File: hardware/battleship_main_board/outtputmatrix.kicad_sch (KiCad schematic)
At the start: 0 parts

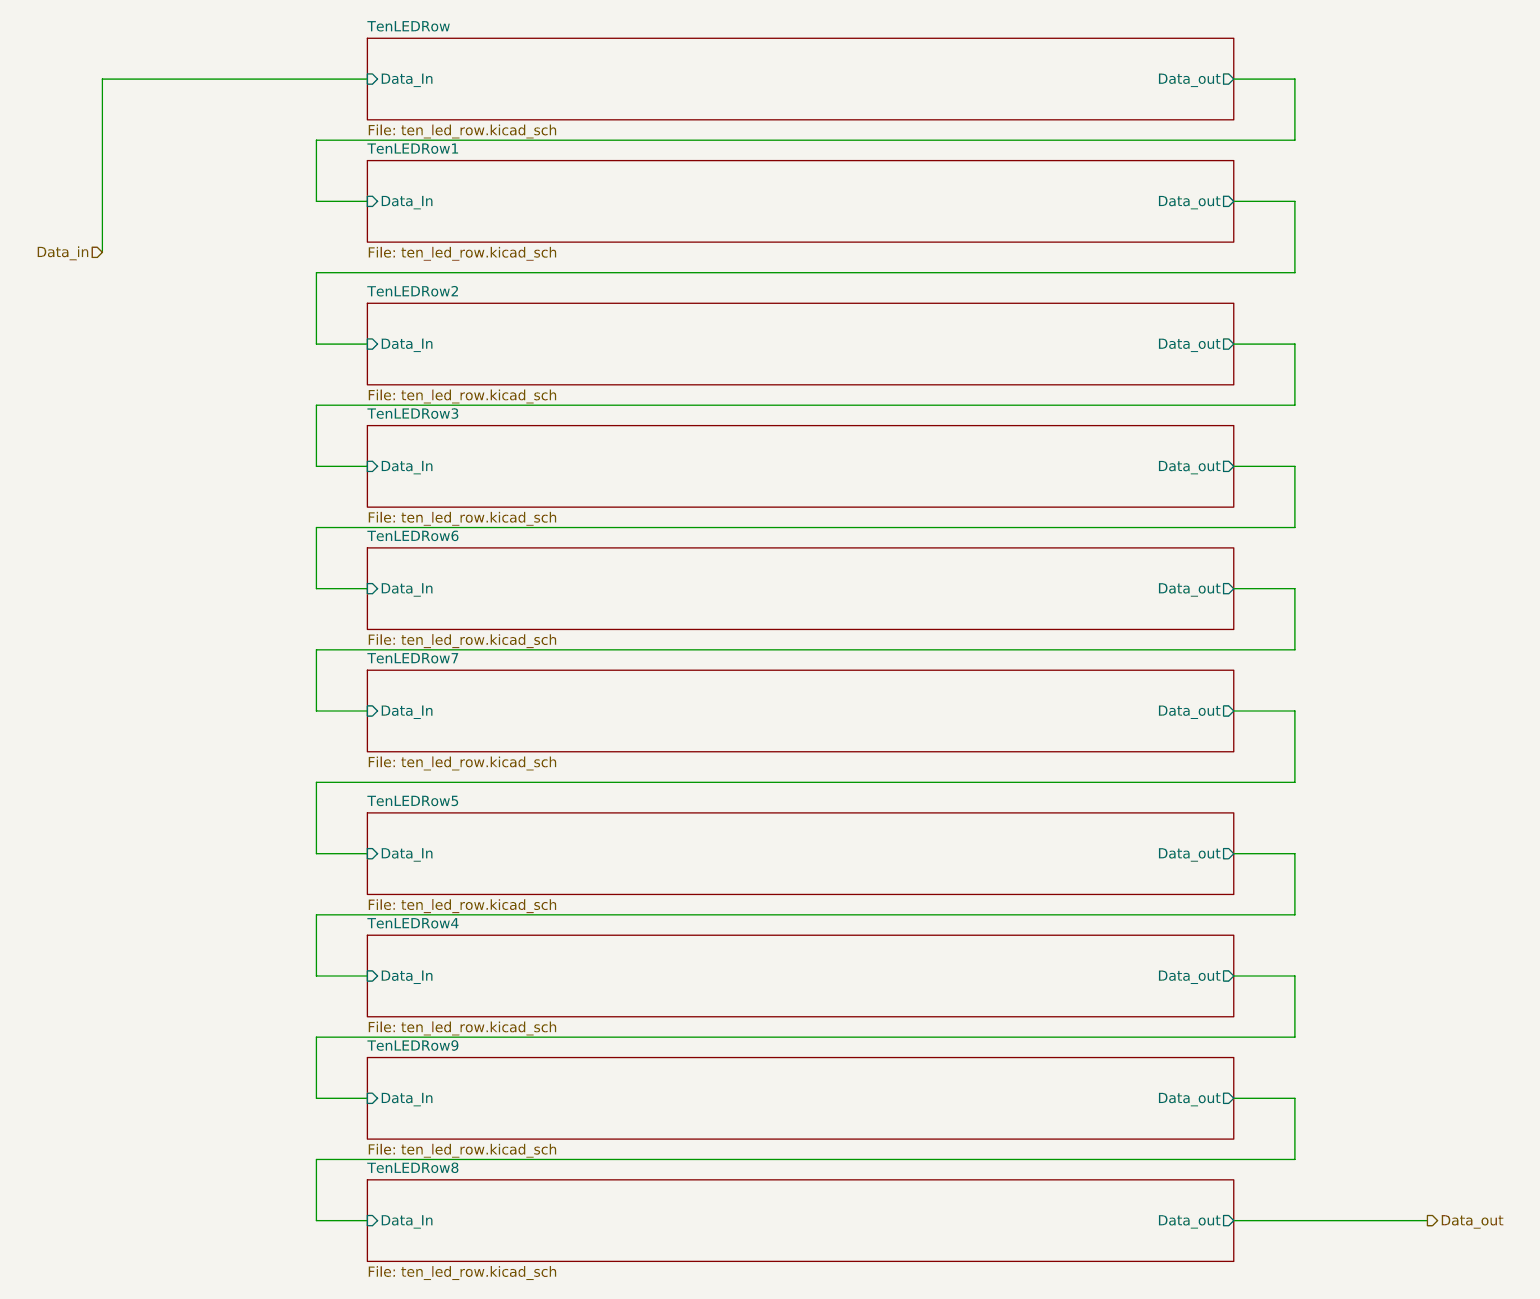
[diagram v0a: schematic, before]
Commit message: Got schematic to place that can be turned into a ratsnest
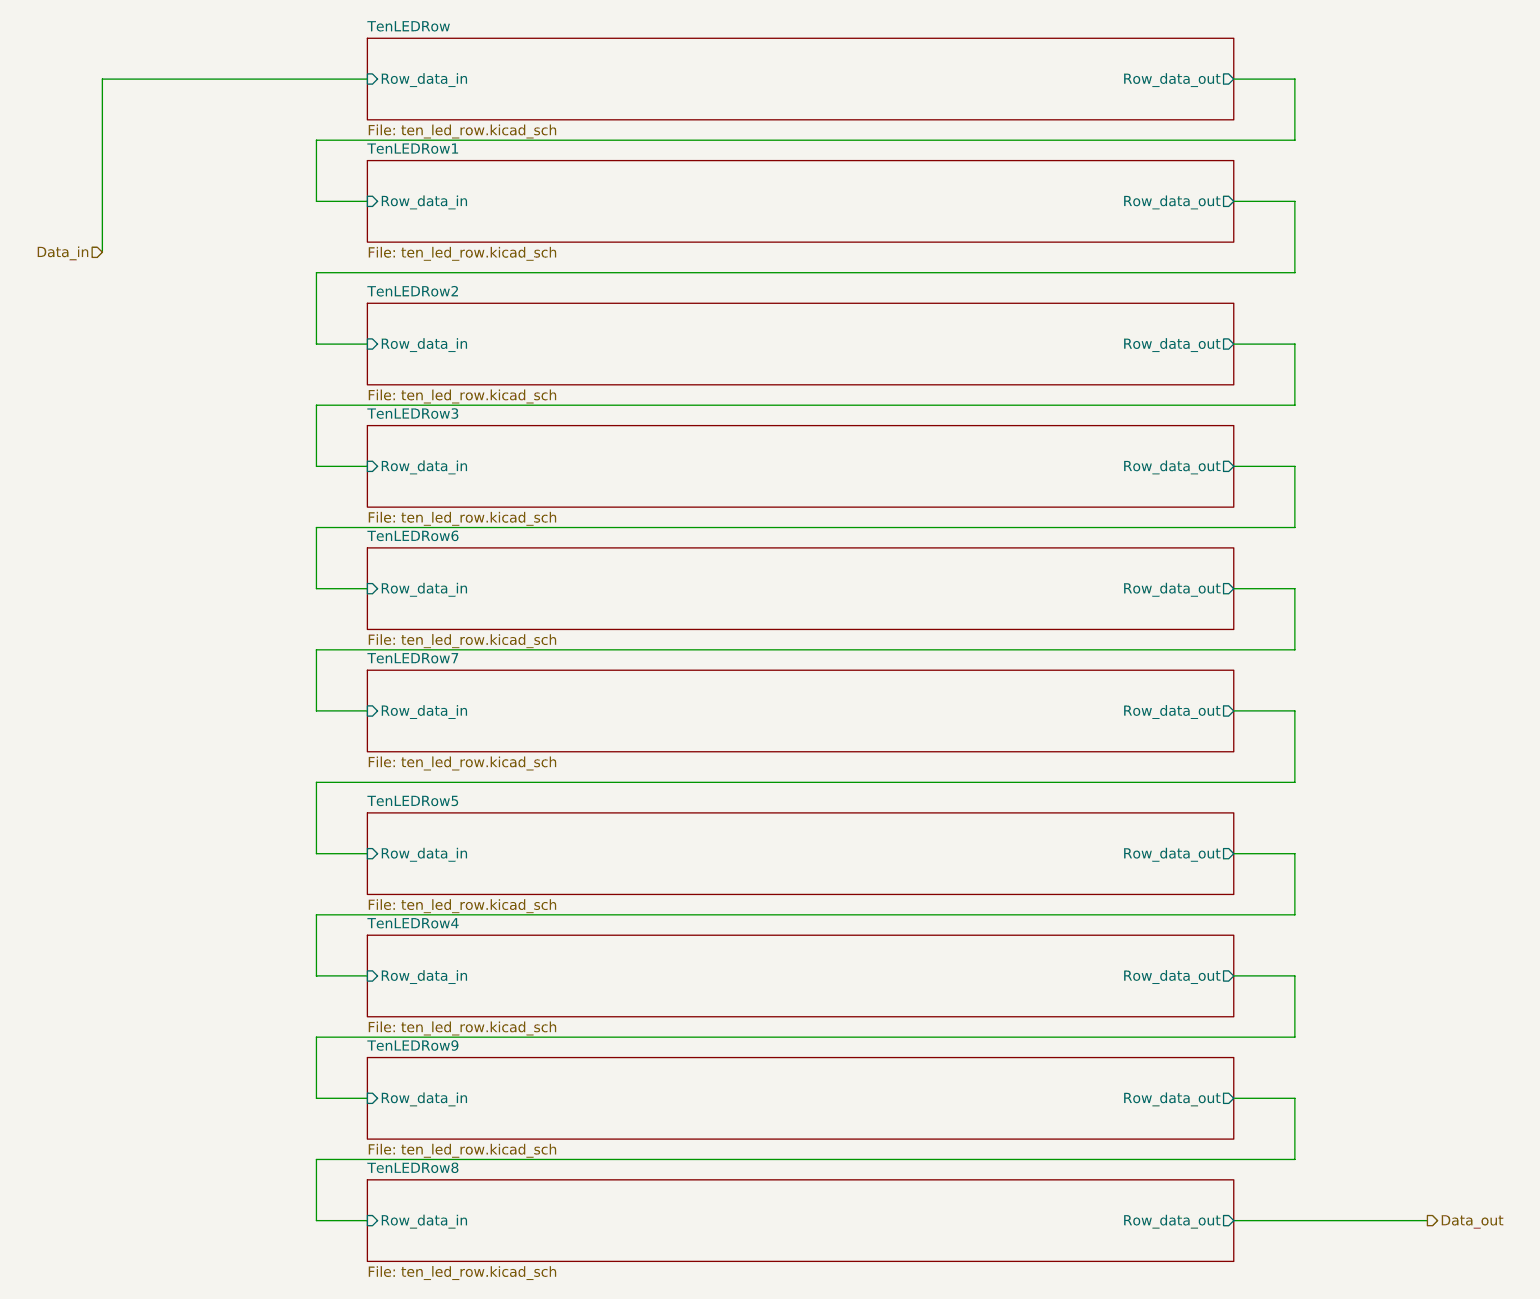
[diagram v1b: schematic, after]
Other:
- sheet TenLEDRow ports: added Row_data_in, Row_data_out; removed Data_In, Data_out
- sheet TenLEDRow1 ports: added Row_data_in, Row_data_out; removed Data_In, Data_out
- sheet TenLEDRow2 ports: added Row_data_in, Row_data_out; removed Data_In, Data_out
- sheet TenLEDRow3 ports: added Row_data_in, Row_data_out; removed Data_In, Data_out
- sheet TenLEDRow4 ports: added Row_data_in, Row_data_out; removed Data_In, Data_out
- sheet TenLEDRow5 ports: added Row_data_in, Row_data_out; removed Data_In, Data_out
- sheet TenLEDRow6 ports: added Row_data_in, Row_data_out; removed Data_In, Data_out
- sheet TenLEDRow7 ports: added Row_data_in, Row_data_out; removed Data_In, Data_out
- sheet TenLEDRow8 ports: added Row_data_in, Row_data_out; removed Data_In, Data_out
- sheet TenLEDRow9 ports: added Row_data_in, Row_data_out; removed Data_In, Data_out
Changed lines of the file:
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@@
       (effects (font (size 1.27 1.27)) (justify left top))
     )
-    (pin "Data_out" output (at 165.1 85.09 0)
+    (pin "Row_data_out" output (at 165.1 85.09 0)
       (effects (font (size 1.27 1.27)) (justify right))
     )
-    (pin "Data_In" input (at 57.15 85.09 180)
+    (pin "Row_data_in" input (at 57.15 85.09 180)
       (effects (font (size 1.27 1.27)) (justify left))
     )
@@
       (effects (font (size 1.27 1.27)) (justify left top))
     )
-    (pin "Data_out" output (at 165.1 148.59 0)
+    (pin "Row_data_out" output (at 165.1 148.59 0)
       (effects (font (size 1.27 1.27)) (justify right))
     )
-    (pin "Data_In" input (at 57.15 148.59 180)
+    (pin "Row_data_in" input (at 57.15 148.59 180)
       (effects (font (size 1.27 1.27)) (justify left))
     )
@@
       (effects (font (size 1.27 1.27)) (justify left top))
     )
-    (pin "Data_out" output (at 165.1 133.35 0)
+    (pin "Row_data_out" output (at 165.1 133.35 0)
       (effects (font (size 1.27 1.27)) (justify right))
     )
-    (pin "Data_In" input (at 57.15 133.35 180)
+    (pin "Row_data_in" input (at 57.15 133.35 180)
       (effects (font (size 1.27 1.27)) (justify left))
     )
@@
       (effects (font (size 1.27 1.27)) (justify left top))
     )
-    (pin "Data_out" output (at 165.1 69.85 0)
+    (pin "Row_data_out" output (at 165.1 69.85 0)
       (effects (font (size 1.27 1.27)) (justify right))
     )
-    (pin "Data_In" input (at 57.15 69.85 180)
+    (pin "Row_data_in" input (at 57.15 69.85 180)
       (effects (font (size 1.27 1.27)) (justify left))
     )
@@
       (effects (font (size 1.27 1.27)) (justify left top))
     )
-    (pin "Data_out" output (at 165.1 21.59 0)
+    (pin "Row_data_out" output (at 165.1 21.59 0)
       (effects (font (size 1.27 1.27)) (justify right))
     )
-    (pin "Data_In" input (at 57.15 21.59 180)
+    (pin "Row_data_in" input (at 57.15 21.59 180)
       (effects (font (size 1.27 1.27)) (justify left))
     )
@@
       (effects (font (size 1.27 1.27)) (justify left top))
     )
-    (pin "Data_out" output (at 165.1 36.83 0)
+    (pin "Row_data_out" output (at 165.1 36.83 0)
       (effects (font (size 1.27 1.27)) (justify right))
     )
-    (pin "Data_In" input (at 57.15 36.83 180)
+    (pin "Row_data_in" input (at 57.15 36.83 180)
       (effects (font (size 1.27 1.27)) (justify left))
     )
@@
       (effects (font (size 1.27 1.27)) (justify left top))
     )
-    (pin "Data_out" output (at 165.1 54.61 0)
+    (pin "Row_data_out" output (at 165.1 54.61 0)
       (effects (font (size 1.27 1.27)) (justify right))
     )
-    (pin "Data_In" input (at 57.15 54.61 180)
+    (pin "Row_data_in" input (at 57.15 54.61 180)
       (effects (font (size 1.27 1.27)) (justify left))
     )
@@
       (effects (font (size 1.27 1.27)) (justify left top))
     )
-    (pin "Data_out" output (at 165.1 100.33 0)
+    (pin "Row_data_out" output (at 165.1 100.33 0)
       (effects (font (size 1.27 1.27)) (justify right))
     )
-    (pin "Data_In" input (at 57.15 100.33 180)
+    (pin "Row_data_in" input (at 57.15 100.33 180)
       (effects (font (size 1.27 1.27)) (justify left))
     )
@@
       (effects (font (size 1.27 1.27)) (justify left top))
     )
-    (pin "Data_out" output (at 165.1 118.11 0)
+    (pin "Row_data_out" output (at 165.1 118.11 0)
       (effects (font (size 1.27 1.27)) (justify right))
     )
-    (pin "Data_In" input (at 57.15 118.11 180)
+    (pin "Row_data_in" input (at 57.15 118.11 180)
       (effects (font (size 1.27 1.27)) (justify left))
     )
@@
       (effects (font (size 1.27 1.27)) (justify left top))
     )
-    (pin "Data_out" output (at 165.1 163.83 0)
+    (pin "Row_data_out" output (at 165.1 163.83 0)
       (effects (font (size 1.27 1.27)) (justify right))
     )
-    (pin "Data_In" input (at 57.15 163.83 180)
+    (pin "Row_data_in" input (at 57.15 163.83 180)
       (effects (font (size 1.27 1.27)) (justify left))
     )
